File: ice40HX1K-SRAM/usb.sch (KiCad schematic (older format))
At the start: 4 parts

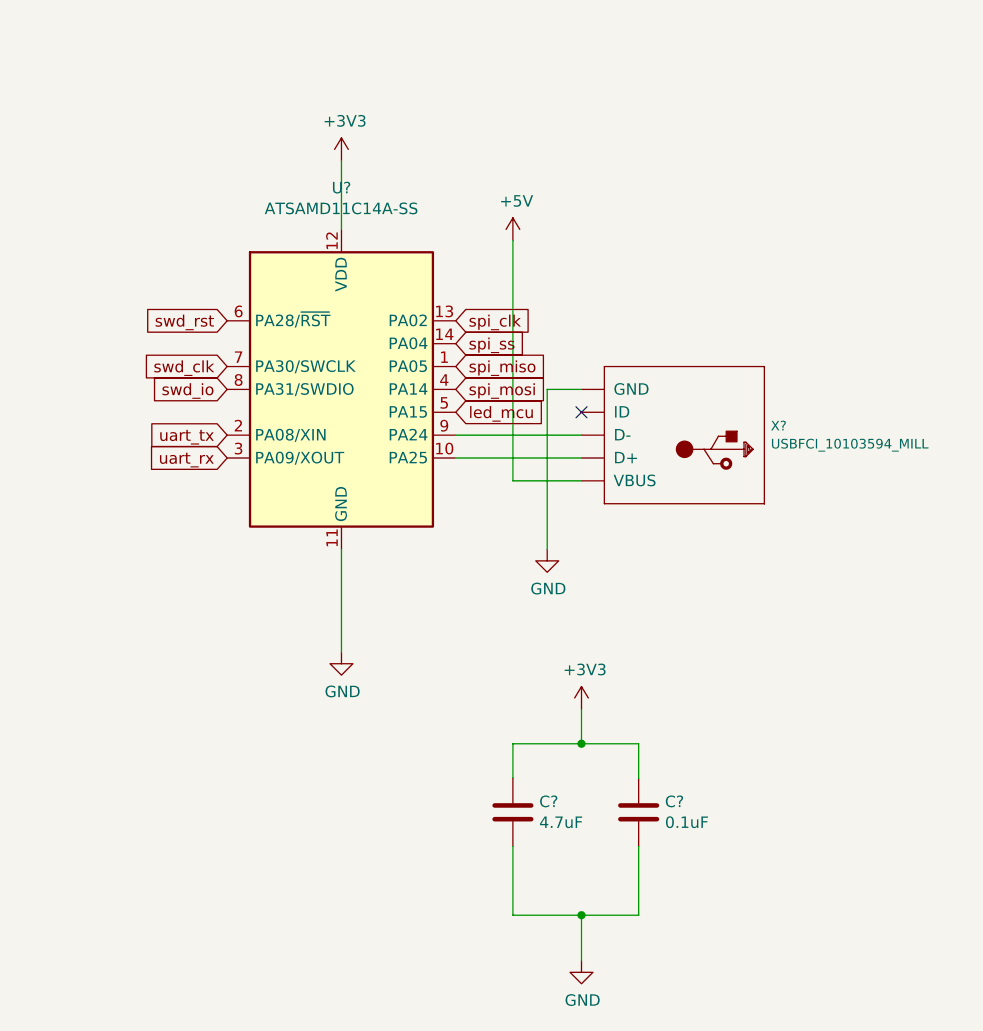
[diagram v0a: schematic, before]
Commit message: add nRF52 module for FPGA programming
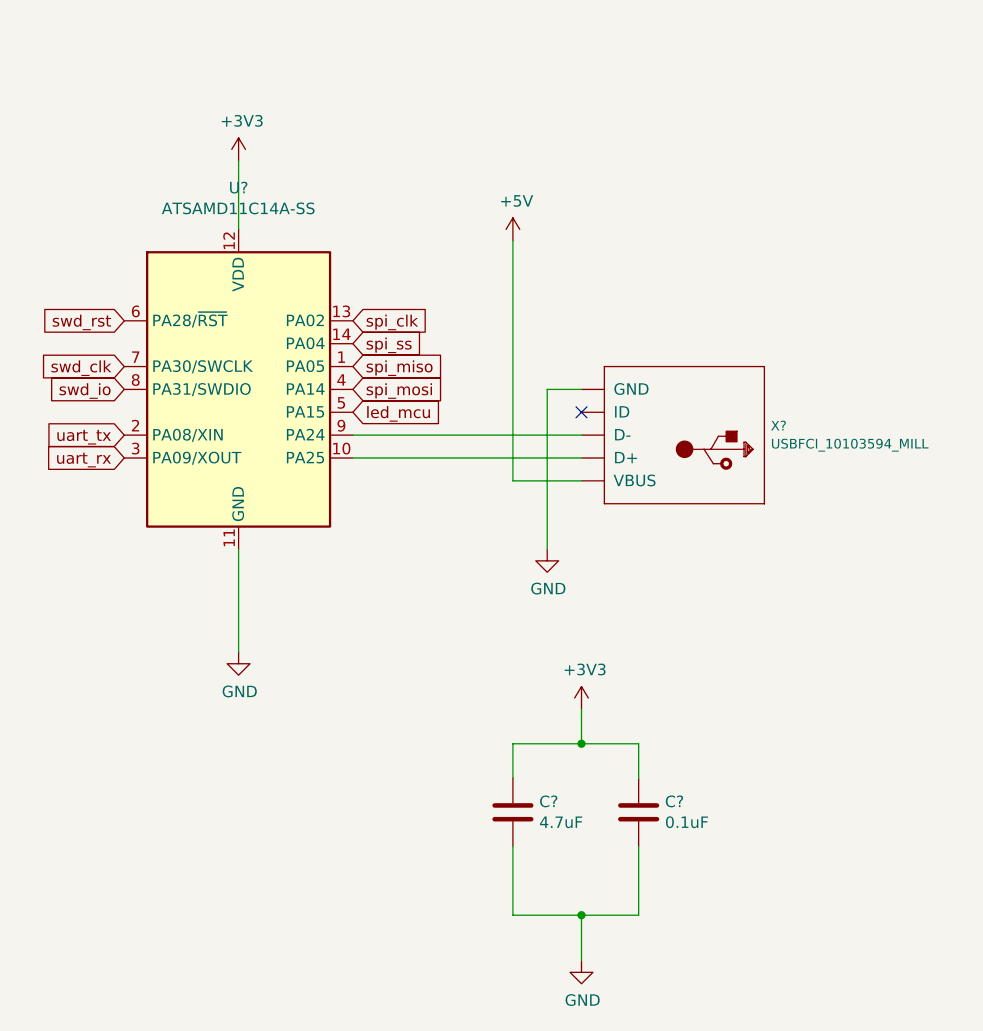
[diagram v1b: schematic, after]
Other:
- moved on the sheet: U?
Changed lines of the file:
@@
 L GitRep_SAMD:ATSAMD11C14A-SS U?
 U 1 1 5E5FB16F
-P 3450 2500
-F 0 "U?" H 3450 3381 50  0000 C CNN
-F 1 "ATSAMD11C14A-SS" H 3450 3290 50  0000 C CNN
-F 2 "Package_SO:SOIC-14_3.9x8.7mm_P1.27mm" H 3450 1450 50  0001 C CNN
-F 3 "http://ww1.microchip.com/downloads/en/DeviceDoc/Atmel-42363-SAM-D11_Datasheet.pdf" H 3450 1800 50  0001 C CNN
-	1    3450 2500
+P 3000 2500
+F 0 "U?" H 3000 3381 50  0000 C CNN
+F 1 "ATSAMD11C14A-SS" H 3000 3290 50  0000 C CNN
+F 2 "Package_SO:SOIC-14_3.9x8.7mm_P1.27mm" H 3000 1450 50  0001 C CNN
+F 3 "http://ww1.microchip.com/downloads/en/DeviceDoc/Atmel-42363-SAM-D11_Datasheet.pdf" H 3000 1800 50  0001 C CNN
+	1    3000 2500
 	1    0    0    -1
 $EndComp
@@
 	-1   0    0    1
 $EndComp
-Wire Wire Line
-	3950 2700 4500 2700
-Wire Wire Line
-	3950 2800 4500 2800
-Text GLabel 2950 2700 0    50   Input ~ 0
+Text GLabel 2500 2700 0    50   Input ~ 0
 uart_tx
-Text GLabel 2950 2800 0    50   Input ~ 0
+Text GLabel 2500 2800 0    50   Input ~ 0
 uart_rx
 $Comp
@@
 L power:GND #PWR?
 U 1 1 5E603984
-P 3450 3650
-F 0 "#PWR?" H 3450 3400 50  0001 C CNN
-F 1 "GND" H 3455 3477 50  0000 C CNN
-F 2 "" H 3450 3650 50  0001 C CNN
-F 3 "" H 3450 3650 50  0001 C CNN
-	1    3450 3650
+P 3000 3650
+F 0 "#PWR?" H 3000 3400 50  0001 C CNN
+F 1 "GND" H 3005 3477 50  0000 C CNN
+F 2 "" H 3000 3650 50  0001 C CNN
+F 3 "" H 3000 3650 50  0001 C CNN
+	1    3000 3650
 	1    0    0    -1
 $EndComp
@@
 L power:+3V3 #PWR?
 U 1 1 5E604967
-P 3450 1500
-F 0 "#PWR?" H 3450 1350 50  0001 C CNN
-F 1 "+3V3" H 3465 1673 50  0000 C CNN
-F 2 "" H 3450 1500 50  0001 C CNN
-F 3 "" H 3450 1500 50  0001 C CNN
-	1    3450 1500
+P 3000 1500
+F 0 "#PWR?" H 3000 1350 50  0001 C CNN
+F 1 "+3V3" H 3015 1673 50  0000 C CNN
+F 2 "" H 3000 1500 50  0001 C CNN
+F 3 "" H 3000 1500 50  0001 C CNN
+	1    3000 1500
 	1    0    0    -1
 $EndComp
@@
 	4200 2900 4500 2900
 Wire Wire Line
-	3450 3650 3450 3200
+	3000 3650 3000 3200
 Wire Wire Line
-	3450 1500 3450 1800
+	3000 1500 3000 1800
 Wire Wire Line
 	4500 2500 4350 2500
@@
 	4350 2500 4350 3200
 NoConn ~ 4500 2600
-Text GLabel 2950 2200 0    50   Input ~ 0
+Text GLabel 2500 2200 0    50   Input ~ 0
 swd_rst
-Text GLabel 2950 2400 0    50   Input ~ 0
+Text GLabel 2500 2400 0    50   Input ~ 0
 swd_clk
-Text GLabel 2950 2500 0    50   Input ~ 0
+Text GLabel 2500 2500 0    50   Input ~ 0
 swd_io
-Text GLabel 3950 2200 2    50   Input ~ 0
+Text GLabel 3500 2200 2    50   Input ~ 0
 spi_clk
-Text GLabel 3950 2300 2    50   Input ~ 0
+Text GLabel 3500 2300 2    50   Input ~ 0
 spi_ss
-Text GLabel 3950 2400 2    50   Input ~ 0
+Text GLabel 3500 2400 2    50   Input ~ 0
 spi_miso
-Text GLabel 3950 2500 2    50   Input ~ 0
+Text GLabel 3500 2500 2    50   Input ~ 0
 spi_mosi
-Text GLabel 3950 2600 2    50   Input ~ 0
+Text GLabel 3500 2600 2    50   Input ~ 0
 led_mcu
+Wire Wire Line
+	3500 2700 4500 2700
+Wire Wire Line
+	3500 2800 4500 2800
 $EndSCHEMATC

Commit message: add ASE-10.000MHZ XTAL
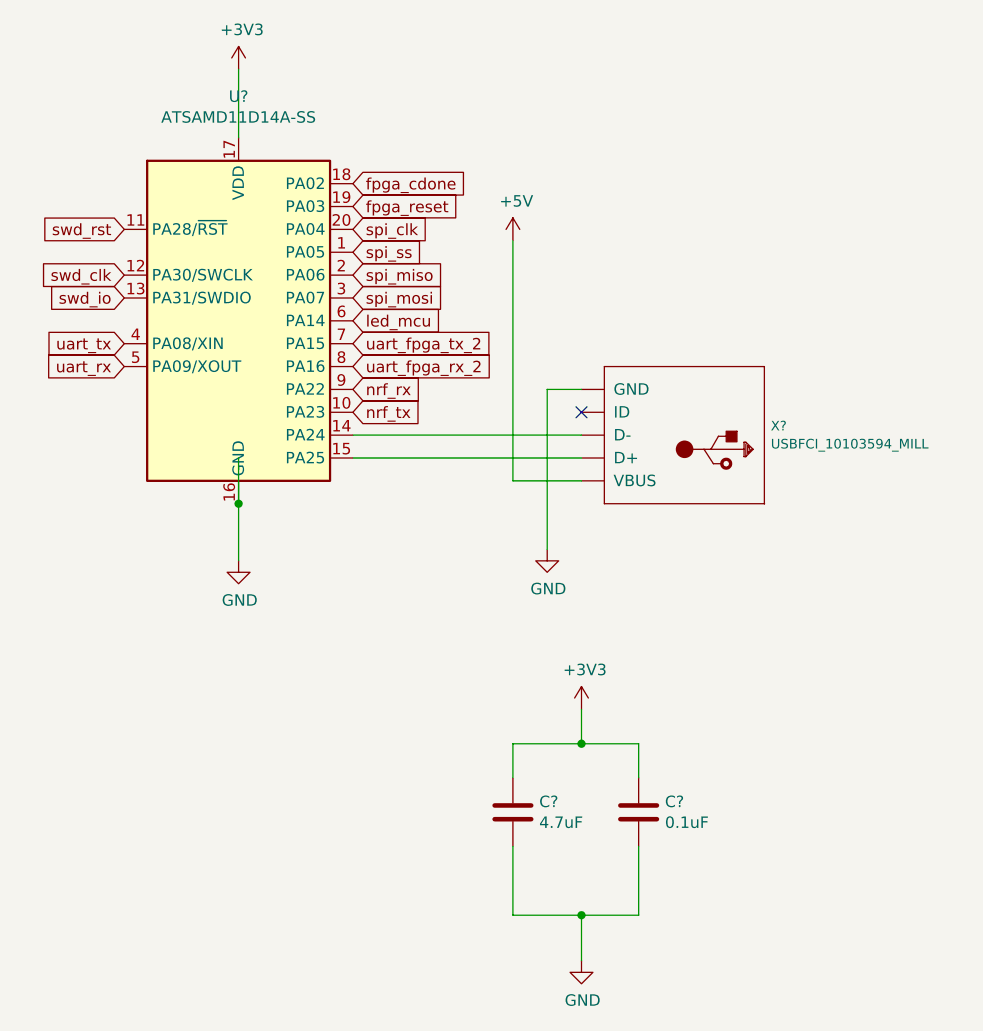
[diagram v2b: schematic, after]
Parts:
- removed U?: ATSAMD11C14A-SS, Package_SO:SOIC-14_3.9x8.7mm_P1.27mm, symbol GitRep_SAMD:ATSAMD11C14A-SS
- added U?: ATSAMD11D14A-SS, Package_SO:SOIC-20W_7.5x12.8mm_P1.27mm, symbol GitRep_SAMD:ATSAMD11D14A-SS
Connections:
- net labels added: fpga_cdone, fpga_reset, nrf_rx, nrf_tx, uart_fpga_rx_2, uart_fpga_tx_2
- wire segments 18 -> 19
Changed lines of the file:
@@
 $Descr A4 11693 8268
 encoding utf-8
-Sheet 7 8
+Sheet 7 9
 Title ""
 Date ""
@@
 Comment4 ""
 $EndDescr
-$Comp
-L GitRep_SAMD:ATSAMD11C14A-SS U?
-U 1 1 5E5FB16F
-P 3000 2500
-F 0 "U?" H 3000 3381 50  0000 C CNN
-F 1 "ATSAMD11C14A-SS" H 3000 3290 50  0000 C CNN
-F 2 "Package_SO:SOIC-14_3.9x8.7mm_P1.27mm" H 3000 1450 50  0001 C CNN
-F 3 "http://ww1.microchip.com/downloads/en/DeviceDoc/Atmel-42363-SAM-D11_Datasheet.pdf" H 3000 1800 50  0001 C CNN
-	1    3000 2500
-	1    0    0    -1
-$EndComp
 $Comp
 L cyUsb:USBFCI_10103594_MILL X?
@@
 	-1   0    0    1
 $EndComp
-Text GLabel 2500 2700 0    50   Input ~ 0
+Text GLabel 2500 2300 0    50   Input ~ 0
 uart_tx
-Text GLabel 2500 2800 0    50   Input ~ 0
+Text GLabel 2500 2400 0    50   Input ~ 0
 uart_rx
 $Comp
@@
 $Comp
 L power:GND #PWR?
-U 1 1 5E603984
-P 3000 3650
-F 0 "#PWR?" H 3000 3400 50  0001 C CNN
-F 1 "GND" H 3005 3477 50  0000 C CNN
-F 2 "" H 3000 3650 50  0001 C CNN
-F 3 "" H 3000 3650 50  0001 C CNN
-	1    3000 3650
-	1    0    0    -1
-$EndComp
-$Comp
-L power:GND #PWR?
 U 1 1 5E6043F3
 P 4350 3200
@@
 L power:+3V3 #PWR?
 U 1 1 5E604967
-P 3000 1500
-F 0 "#PWR?" H 3000 1350 50  0001 C CNN
-F 1 "+3V3" H 3015 1673 50  0000 C CNN
-F 2 "" H 3000 1500 50  0001 C CNN
-F 3 "" H 3000 1500 50  0001 C CNN
-	1    3000 1500
+P 3000 1100
+F 0 "#PWR?" H 3000 950 50  0001 C CNN
+F 1 "+3V3" H 3015 1273 50  0000 C CNN
+F 2 "" H 3000 1100 50  0001 C CNN
+F 3 "" H 3000 1100 50  0001 C CNN
+	1    3000 1100
 	1    0    0    -1
 $EndComp
@@
 	4200 2900 4500 2900
 Wire Wire Line
-	3000 3650 3000 3200
-Wire Wire Line
-	3000 1500 3000 1800
+	3000 1100 3000 1400
 Wire Wire Line
 	4500 2500 4350 2500
@@
 	4350 2500 4350 3200
 NoConn ~ 4500 2600
-Text GLabel 2500 2200 0    50   Input ~ 0
+Text GLabel 2500 1800 0    50   Input ~ 0
 swd_rst
-Text GLabel 2500 2400 0    50   Input ~ 0
+Text GLabel 2500 2000 0    50   Input ~ 0
 swd_clk
-Text GLabel 2500 2500 0    50   Input ~ 0
+Text GLabel 2500 2100 0    50   Input ~ 0
 swd_io
+Text GLabel 3500 1800 2    50   Input ~ 0
+spi_clk
+Text GLabel 3500 1900 2    50   Input ~ 0
+spi_ss
+Text GLabel 3500 2000 2    50   Input ~ 0
+spi_miso
+Text GLabel 3500 2100 2    50   Input ~ 0
+spi_mosi
 Text GLabel 3500 2200 2    50   Input ~ 0
-spi_clk
-Text GLabel 3500 2300 2    50   Input ~ 0
-spi_ss
-Text GLabel 3500 2400 2    50   Input ~ 0
-spi_miso
-Text GLabel 3500 2500 2    50   Input ~ 0
-spi_mosi
-Text GLabel 3500 2600 2    50   Input ~ 0
 led_mcu
+$Comp
+L GitRep_SAMD:ATSAMD11D14A-SS U?
+U 1 1 5E657B17
+P 3000 2200
+F 0 "U?" H 3000 3181 50  0000 C CNN
+F 1 "ATSAMD11D14A-SS" H 3000 3090 50  0000 C CNN
+F 2 "Package_SO:SOIC-20W_7.5x12.8mm_P1.27mm" H 3000 1050 50  0001 C CNN
+F 3 "http://ww1.microchip.com/downloads/en/DeviceDoc/Atmel-42363-SAM-D11_Datasheet.pdf" H 3000 1300 50  0001 C CNN
+	1    3000 2200
+	1    0    0    -1
+$EndComp
 Wire Wire Line
 	3500 2700 4500 2700
 Wire Wire Line
-	3500 2800 4500 2800
+	4500 2800 3500 2800
+$Comp
+L power:GND #PWR?
+U 1 1 5E603984
+P 3000 3250
+F 0 "#PWR?" H 3000 3000 50  0001 C CNN
+F 1 "GND" H 3005 3077 50  0000 C CNN
+F 2 "" H 3000 3250 50  0001 C CNN
+F 3 "" H 3000 3250 50  0001 C CNN
+	1    3000 3250
+	1    0    0    -1
+$EndComp
+Wire Wire Line
+	3000 3000 3000 2800
+Wire Wire Line
+	3000 3250 3000 3000
+Connection ~ 3000 3000
+Text GLabel 3500 1700 2    50   Input ~ 0
+fpga_reset
+Text GLabel 3500 1600 2    50   Input ~ 0
+fpga_cdone
+Text GLabel 3500 2300 2    50   Input ~ 0
+uart_fpga_tx_2
+Text GLabel 3500 2400 2    50   Input ~ 0
+uart_fpga_rx_2
+Text GLabel 3500 2500 2    50   Input ~ 0
+nrf_rx
+Text GLabel 3500 2600 2    50   Input ~ 0
+nrf_tx
 $EndSCHEMATC
